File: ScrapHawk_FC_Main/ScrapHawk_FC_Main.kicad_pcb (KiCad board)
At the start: 2 copper layers, 40 x 40 mm, 51 parts, among them IC1 MP1584EN-LF-Z, J1 USB_C_Receptacle_USB2.0_16P, U1 RP2040, U2 W25Q128JVS, U3 AMS1117CD-3.3, U4 LSM6DS3TR, Y1 12M

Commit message: wire pcb place components
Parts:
- added J2: Conn_01x06, Connector_JST:JST_SH_BM06B-SRSS-TB_1x06-1MP_P1.00mm_Vertical, F.Cu at (49.5, 32.2)
- moved D4 28.8 mm to (72.5, 48.0), turned to 0 degrees
- moved D3 25.5 mm to (72.8, 44.2), turned to 180 degrees
- moved U2 1.75 mm to (60.8, 36.0), turned to -135 degrees
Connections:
- U1 pad 2: unconnected-(U1-GPIO0-Pad2) -> UART0_TX
- U1 pad 3: LED1 -> UART0_RX
- U1 pad 4: LED2 -> unconnected-(U1-GPIO2-Pad4)
- U1 pad 6: unconnected-(U1-GPIO4-Pad6) -> I2C0_SDA
- U1 pad 7: unconnected-(U1-GPIO5-Pad7) -> I2C0_SCL

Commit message: finish pcb wiring
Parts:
- removed the REF** at (40.0, 65.0)
- removed the REF** at (40.0, 35.0)
- removed the REF** at (70.0, 65.0)
- removed the REF** at (70.0, 35.0)
- added J3: Conn_01x06, Connector_JST:JST_SH_BM06B-SRSS-TB_1x06-1MP_P1.00mm_Vertical, F.Cu at (37.7, 55.2)
- added REF**: MountingHole_3.2mm_M3_DIN965_Pad_TopBottom, MountingHole:MountingHole_3.2mm_M3_DIN965_Pad_TopBottom, F.Cu at (70.0, 65.0)
- added REF**: MountingHole_3.2mm_M3_DIN965_Pad_TopBottom, MountingHole:MountingHole_3.2mm_M3_DIN965_Pad_TopBottom, F.Cu at (70.0, 35.0)
- added REF**: MountingHole_3.2mm_M3_DIN965_Pad_TopBottom, MountingHole:MountingHole_3.2mm_M3_DIN965_Pad_TopBottom, F.Cu at (40.0, 35.0)
- added REF**: MountingHole_3.2mm_M3_DIN965_Pad_TopBottom, MountingHole:MountingHole_3.2mm_M3_DIN965_Pad_TopBottom, F.Cu at (40.0, 65.0)
- U2: moved to B.Cu
- moved C29 68.0 mm to (53.8, 52.8), turned to 180 degrees
- moved R12 65.1 mm to (36.8, 47.8)
- moved R11 64.9 mm to (36.8, 41.8)
- moved C28 63.7 mm to (58.0, 50.0), turned to 90 degrees
- moved C18 51.4 mm to (42.8, 58.8), turned to -90 degrees
- moved C24 49.5 mm to (48.8, 56.1), turned to 180 degrees
- moved R8 49.4 mm to (61.8, 61.8)
- moved C21 48.5 mm to (49.0, 46.6)
- moved C16 47.9 mm to (48.8, 57.8)
- moved C19 47.5 mm to (45.5, 57.8)
- moved R6 46.8 mm to (68.5, 60.8), turned to 180 degrees
- moved C23 43.0 mm to (50.8, 36.2), turned to 90 degrees
- moved R7 41.8 mm to (66.8, 53.2), turned to -90 degrees
- moved C14 41.3 mm to (53.2, 47.1)
- moved C22 40.5 mm to (56.9, 47.1)
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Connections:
- U1 pad 11: unconnected-(U1-GPIO8-Pad11) -> MOTOR1
- U1 pad 12: unconnected-(U1-GPIO9-Pad12) -> MOTOR2
- U1 pad 13: unconnected-(U1-GPIO10-Pad13) -> MOTOR3
- U1 pad 14: unconnected-(U1-GPIO11-Pad14) -> MOTOR4
- U1 pad 15: unconnected-(U1-GPIO12-Pad15) -> LED1
- U1 pad 16: unconnected-(U1-GPIO13-Pad16) -> LED2
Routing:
- net +5V: track 0.00 -> 105.5 mm, vias 0 -> 2
- net GND: track 0.00 -> 71.6 mm, vias 0 -> 30
- net +3.3V: track 0.00 -> 68.9 mm, vias 0 -> 12
- net +BATT: track 0.00 -> 38.8 mm, vias 0 -> 3
- net MOTOR2: track 0.00 -> 32.5 mm, vias 0 -> 2
- net MOTOR3: track 0.00 -> 29.7 mm, vias 0 -> 2
- net MOTOR1: track 0.00 -> 28.0 mm, vias 0 -> 2
- net MOTOR4: track 0.00 -> 26.7 mm, vias 0 -> 2
- net LED2: track 0.00 -> 21.1 mm, vias 0 -> 2
- net +1V1: track 0.00 -> 20.4 mm, vias 0 -> 3
- net LED1: track 0.00 -> 17.0 mm, vias 0 -> 2
- net Net-(D2-K): track 0.00 -> 15.2 mm
- net Net-(D1-K): track 0.00 -> 13.9 mm, vias 0 -> 2
- net SCL: track 0.00 -> 11.9 mm, vias 0 -> 2
- net INT1: track 0.00 -> 10.6 mm, vias 0 -> 2
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- added copper zone on In2.Cu, net +3.3V
- added copper zone on F.Cu, net GND
- added copper zone on In1.Cu, net GND
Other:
- copper layers 2 -> 4

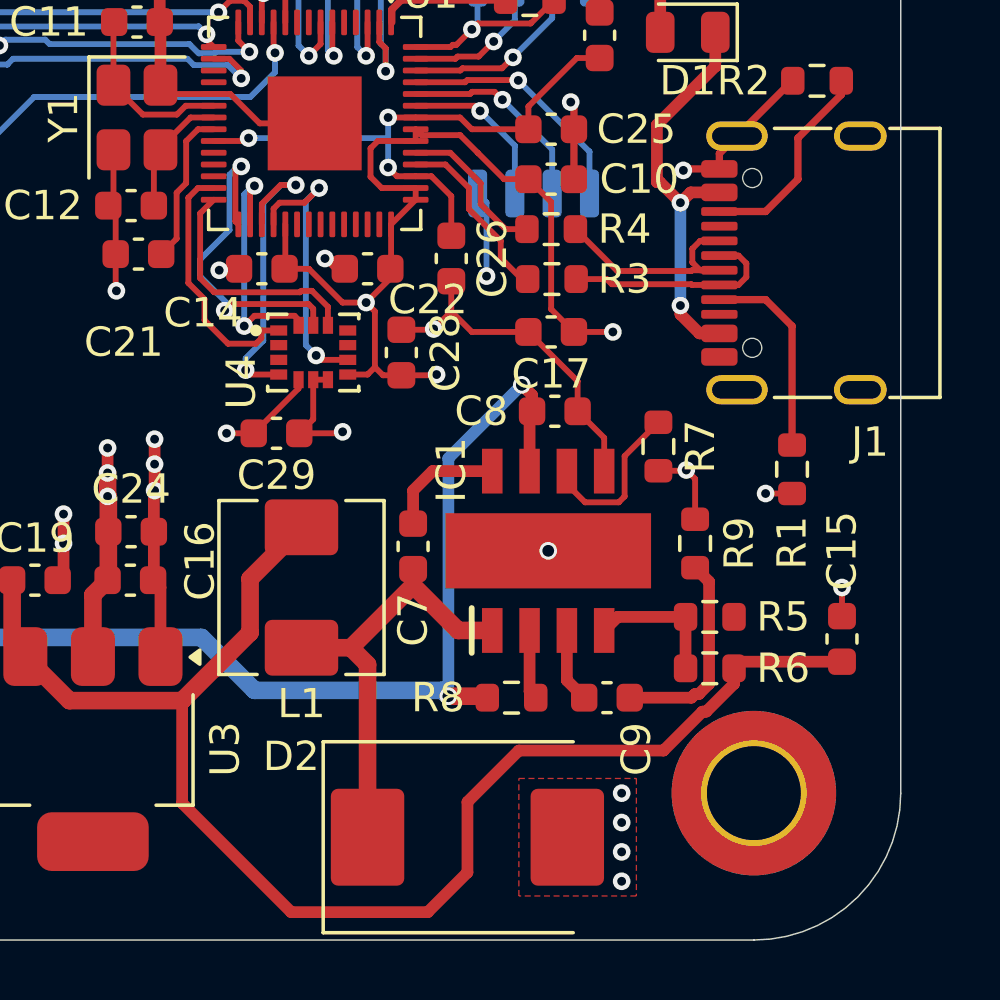
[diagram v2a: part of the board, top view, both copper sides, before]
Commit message: fix capacitors size
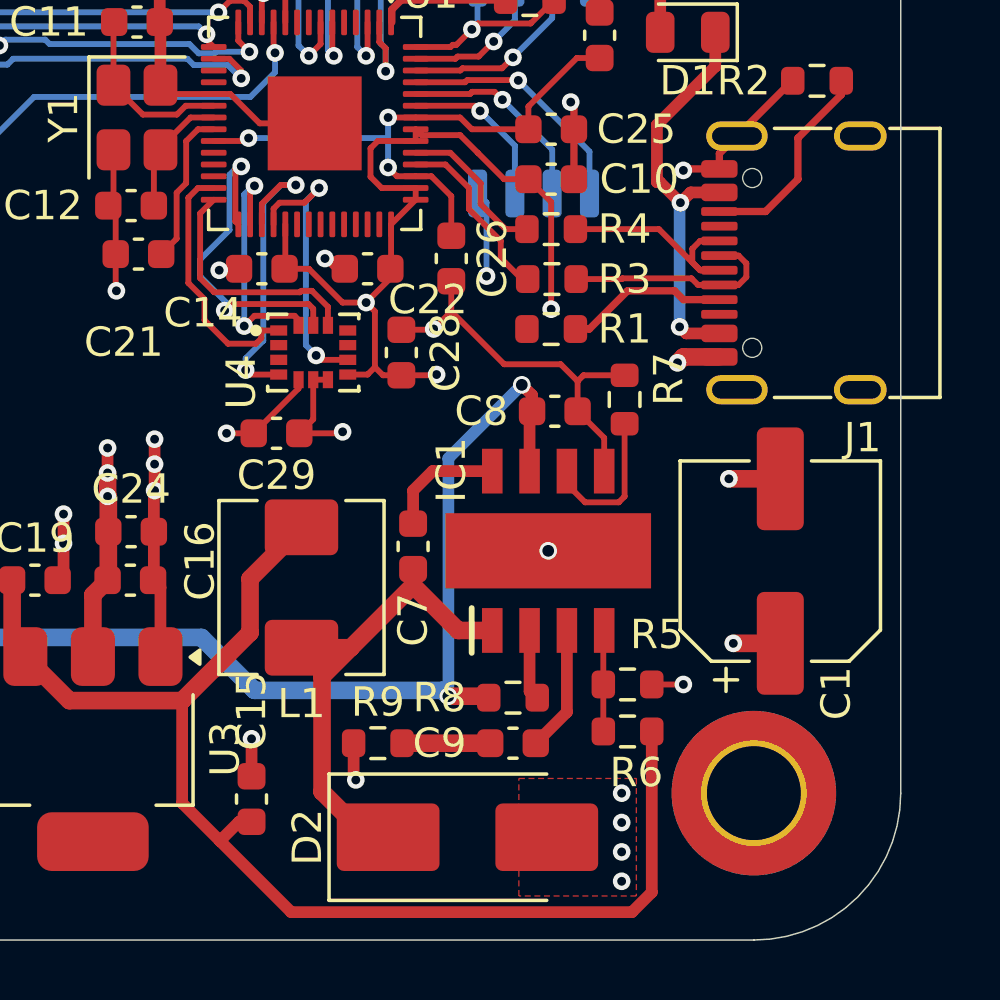
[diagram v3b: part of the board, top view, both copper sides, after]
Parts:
- removed C17: 22p, Capacitor_SMD:C_0603_1608Metric
- added C1: C_Polarized, Capacitor_SMD:CP_Elec_6.3x5.2, F.Cu at (70.9, 57.1)
- C8: value 220p -> 22µF
- D2: footprint Diode_SMD:D_SMC -> Diode_SMD:D_SMB_Handsoldering
- moved C15 20.8 mm to (52.9, 65.2)
- moved R9 12.8 mm to (57.2, 63.3), turned to 180 degrees
- moved R1 9.49 mm to (63.1, 49.2), turned to 180 degrees
- moved R5 3.62 mm to (65.7, 61.3)
- moved C9 3.56 mm to (61.8, 63.3), turned to 0 degrees
- moved R6 3.53 mm to (65.7, 62.9)
- moved R7 1.97 mm to (65.6, 51.6), turned to 90 degrees
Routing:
- net +5V: track 105.5 -> 100.8 mm
- net Net-(C9-Pad1): track 7.05 -> 3.00 mm
- net GND: track 71.6 -> 75.5 mm, vias 30 -> 32
- net Net-(IC1-COMP): track 2.53 -> 4.28 mm
- net Net-(J1-CC1): track 6.90 -> 5.56 mm
- net Net-(IC1-FB): track 4.71 -> 3.45 mm
- net +3.3V: track 68.9 -> 68.1 mm, vias 12 -> 13
- net Net-(D2-K): track 15.2 -> 16.1 mm
- net Net-(IC1-FREQ): track 5.75 -> 5.22 mm

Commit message: update capacitor
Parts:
- added TP1: TestPoint, TestPoint:TestPoint_Pad_D1.5mm, B.Cu at (46.1, 44.2)
- added TP2: TestPoint, TestPoint:TestPoint_Pad_D1.5mm, B.Cu at (46.1, 47.8)
- C8: value 22µF -> 22uF
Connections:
- U1 pad 24: unconnected-(U1-SWCLK-Pad24) -> Net-(U1-SWCLK)
- U1 pad 25: unconnected-(U1-SWDIO-Pad25) -> Net-(U1-SWDIO)
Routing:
- net Net-(U1-SWDIO): track 0.00 -> 9.92 mm, vias 0 -> 1
- net Net-(U1-SWCLK): track 0.00 -> 9.08 mm, vias 0 -> 1
- net SCL: track 11.9 -> 7.90 mm
- net GND: track 75.5 -> 77.1 mm
- net +3.3V: track 68.1 -> 69.4 mm, vias 13 -> 14
- net +1V1: track 20.4 -> 21.4 mm
- net MOSI: track 8.57 -> 7.71 mm

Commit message: update stepdown
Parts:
- removed C15: 22p, Capacitor_SMD:C_0603_1608Metric
- removed C7: 100n, Capacitor_SMD:C_0603_1608Metric
- removed C8: 22uF, Capacitor_SMD:C_0603_1608Metric
- removed C9: 220p, Capacitor_SMD:C_0603_1608Metric
- removed D2: SS34, Diode_SMD:D_SMB_Handsoldering
- removed IC1: MP1584EN-LF-Z, MP1584EN-LF-Z:SOIC127P600X170-9N
- removed L1: 8.2uH, Inductor_SMD:L_Chilisin_BMRA00050520
- removed R5: 10K, Resistor_SMD:R_0603_1608Metric
- removed R6: 52.5K, Resistor_SMD:R_0603_1608Metric
- removed R7: 200K, Resistor_SMD:R_0603_1608Metric
- removed R8, R9: 100K, Resistor_SMD:R_0603_1608Metric
- added C17: 22u, Capacitor_SMD:C_0603_1608Metric, F.Cu at (59.0, 57.1)
- added C30: 0.1u, Capacitor_SMD:C_0603_1608Metric, F.Cu at (62.2, 57.1)
- added C31: 47u, Capacitor_SMD:C_0603_1608Metric, F.Cu at (53.7, 63.8)
- added L2: 4.7uH, Inductor_SMD:L_Chilisin_BMRA00050520, F.Cu at (58.0, 66.5)
- added R13: 52.5K, Resistor_SMD:R_0603_1608Metric, F.Cu at (54.3, 60.4)
- added R14: 52.5K, Resistor_SMD:R_0603_1608Metric, F.Cu at (56.0, 60.4)
- added U5: TPS562200, Package_TO_SOT_SMD:SOT-23-6, F.Cu at (59.0, 60.4)
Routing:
- net +5V: track 100.8 -> 76.7 mm
- net Net-(D2-K): track 16.1 -> 0.00 mm
- net +BATT: track 38.8 -> 26.0 mm, vias 3 -> 2
- net Net-(U5-VBST): track 0.00 -> 10.7 mm
- net Net-(U5-SW): track 0.00 -> 5.50 mm
- net Net-(IC1-FREQ): track 5.22 -> 0.00 mm
- net Net-(IC1-COMP): track 4.28 -> 0.00 mm
- net Net-(IC1-BST): track 4.09 -> 0.00 mm
- net Net-(U5-VFB): track 0.00 -> 3.88 mm
- net GND: track 77.1 -> 73.5 mm, vias 32 -> 27
- net Net-(IC1-FB): track 3.45 -> 0.00 mm
- net Net-(C9-Pad1): track 3.00 -> 0.00 mm
- net Net-(IC1-EN): track 2.37 -> 0.00 mm
- net UART0_TX: track 8.26 -> 7.07 mm
- removed copper zone on F.Cu, net GND

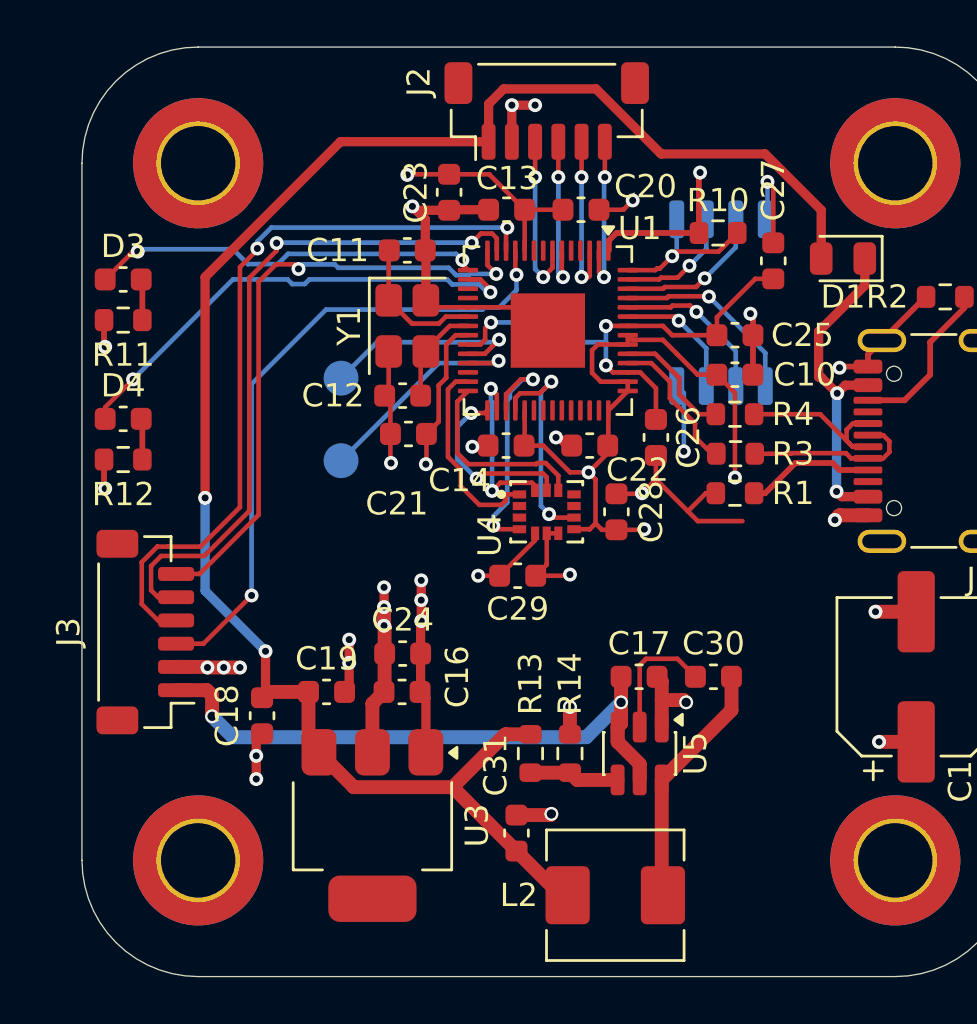
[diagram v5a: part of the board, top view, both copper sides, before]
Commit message: update decoupling capacitor battery
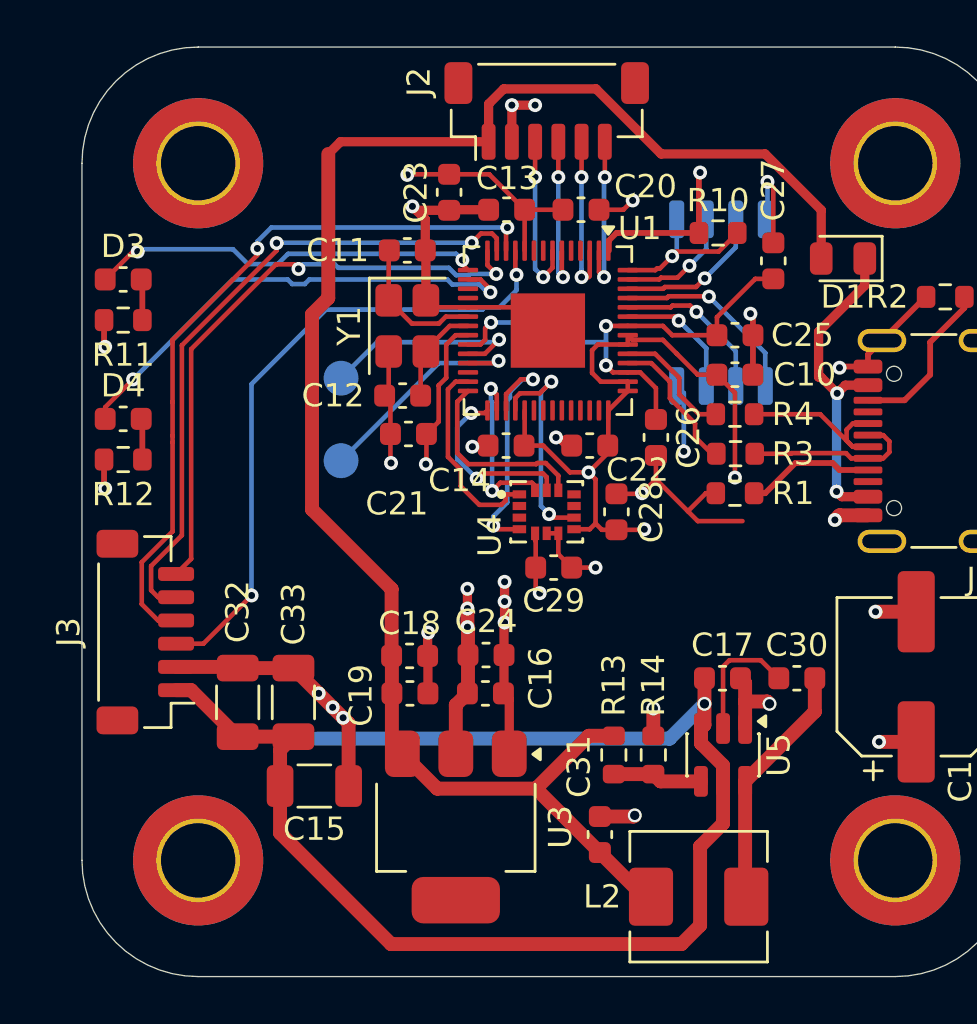
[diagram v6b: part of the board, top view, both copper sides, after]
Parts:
- added C15: 100n, Capacitor_SMD:C_1206_3216Metric, F.Cu at (45.0, 61.8)
- added C32: 100n, Capacitor_SMD:C_1206_3216Metric, F.Cu at (41.7, 58.2)
- added C33: 100n, Capacitor_SMD:C_1206_3216Metric, F.Cu at (44.1, 58.2)
- moved C18 6.85 mm to (49.1, 56.2), turned to 0 degrees
- moved C24 3.59 mm to (52.4, 56.2)
- moved C30 3.59 mm to (65.8, 57.2)
- moved R13 3.59 mm to (57.9, 60.5)
- moved C16 3.59 mm to (52.4, 57.8)
- moved C17 3.59 mm to (62.6, 57.2)
- moved C19 3.59 mm to (49.1, 57.8)
- moved C31 3.59 mm to (57.3, 63.9)
- moved L2 3.59 mm to (61.5, 66.6)
- moved R14 3.59 mm to (59.6, 60.5)
- moved U3 3.59 mm to (51.1, 63.6)
- moved U5 3.59 mm to (62.6, 60.5)
- moved C29 1.59 mm to (55.3, 52.4)
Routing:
- net +BATT: track 26.0 -> 59.5 mm, vias 2 -> 1
- net GND: track 73.5 -> 79.6 mm, vias 27 -> 24
- net +5V: track 76.7 -> 72.8 mm, vias 2 -> 0
- net MOTOR3: track 29.7 -> 28.6 mm
- net MOTOR2: track 32.5 -> 31.5 mm
- net +3.3V: track 69.4 -> 68.7 mm
- net MOTOR4: track 26.7 -> 26.1 mm
